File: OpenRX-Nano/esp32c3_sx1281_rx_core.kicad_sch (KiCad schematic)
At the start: 40 parts, among them U1 ESP32-C3FH4, U2 TLV75533PDQNR, U3 SX1281IMLTRT, U4 RFX2401C, X1 CJ17-400001010B20

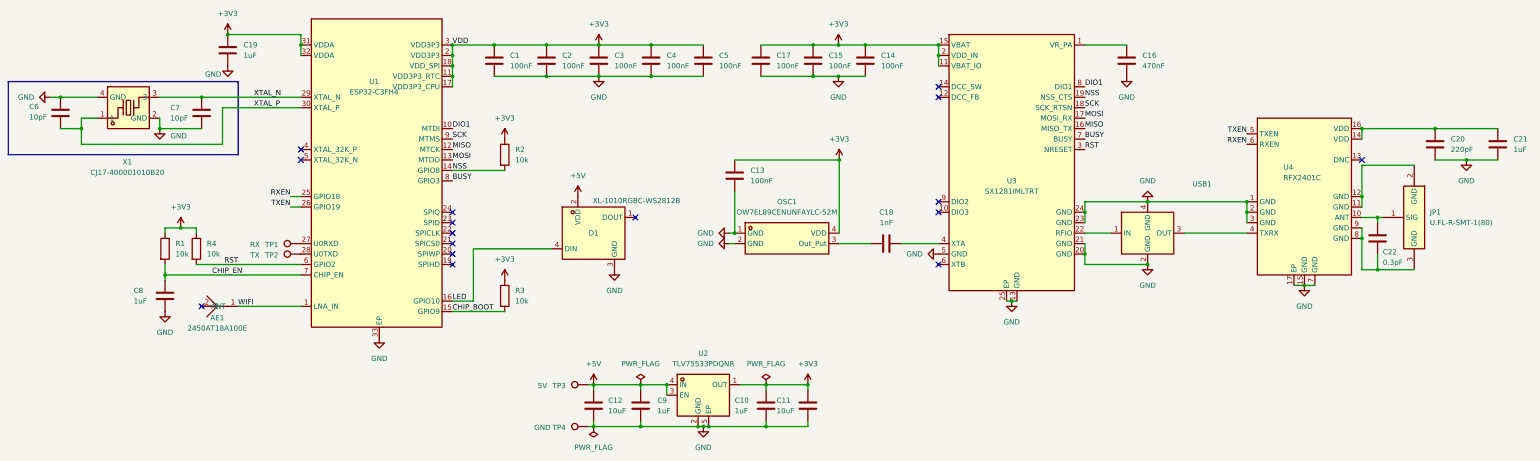
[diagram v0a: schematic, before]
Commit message: Lite + Nano schematics: LCSC fields, fix 10uF to 0402, drop 0.3pF cap
- All passives in both schematics have LCSC fields
- 10uF caps fixed from 0201 to 0402 (C15525)
- Nano C22 (0.3pF): removed discrete cap, use trace capacitance instead
- 0 ERC errors on both schematics
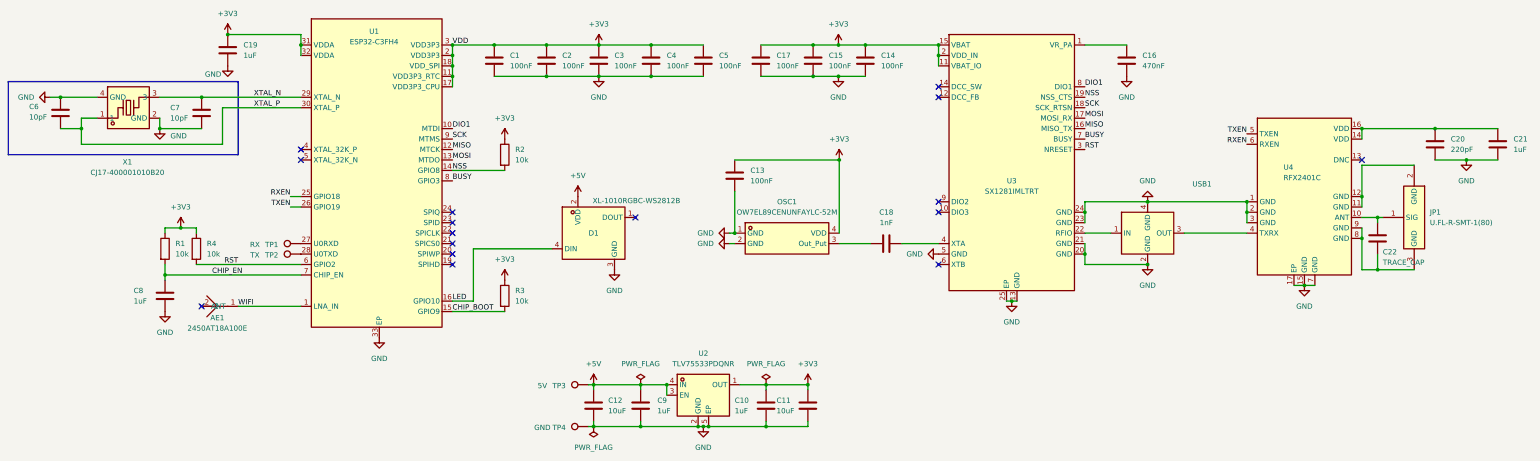
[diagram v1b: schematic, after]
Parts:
- AE1: LCSC (none) -> C89334
- C11, C12: footprint Capacitor_SMD:C_0201_0603Metric -> Capacitor_SMD:C_0402_1005Metric
- C20: LCSC (none) -> C14856
- C22: value 0.3pF -> TRACE_CAP; LCSC (none) -> C1547
- D1: LCSC (none) -> C5349953
- JP1: LCSC (none) -> C88374
- OSC1: LCSC (none) -> C22434896
- U1: LCSC (none) -> C2858491
- U2: LCSC (none) -> C2861882
- U3: LCSC (none) -> C2151551
- U4: LCSC (none) -> C19213
- USB1: LCSC (none) -> C574024
- X1: LCSC (none) -> C2875272
